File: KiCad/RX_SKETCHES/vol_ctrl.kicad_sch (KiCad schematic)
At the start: 6 parts

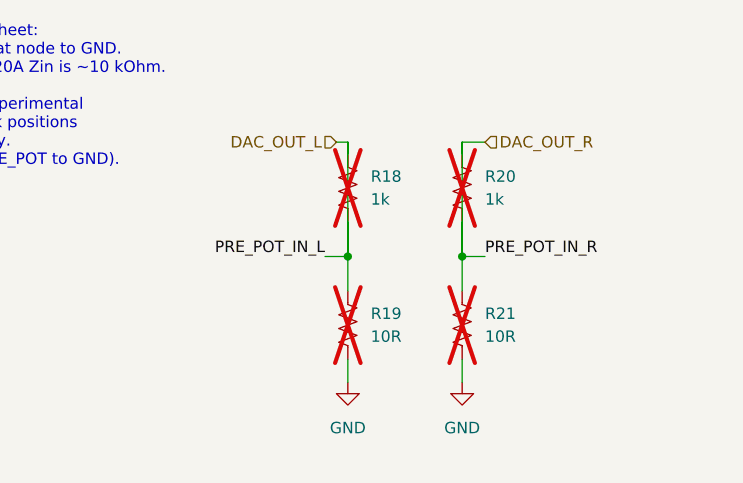
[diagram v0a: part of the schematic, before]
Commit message: WIP: RX schematic review — restore DAC/amp, fix ESP nets, log revisions.
Restore dac/amp from main after rotate damage, rename I2S net to DOUT,
mark amp gain Rs DNP, and record change/rationale in docs/hardware_revisions.org.

Co-authored-by: Cursor <cursoragent@cursor.com>
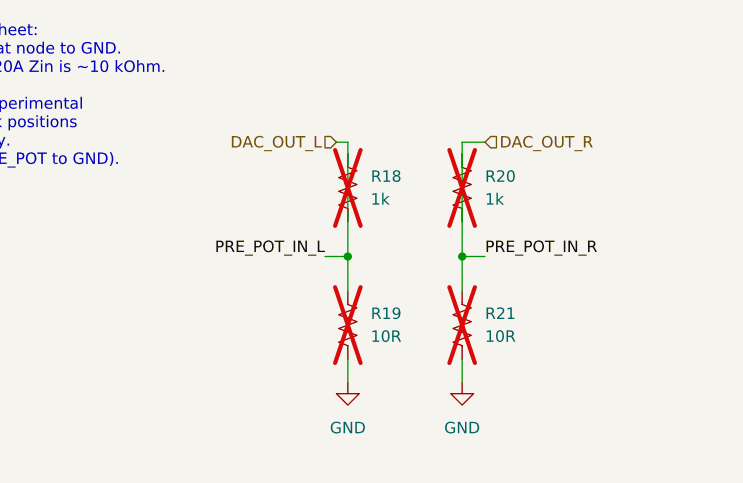
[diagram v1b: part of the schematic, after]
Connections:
- net DAC_OUT_L: no longer R18.1, R18.2
- net DAC_OUT_R: no longer R20.1, R20.2
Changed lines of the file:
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@@
 		(comment 4 "POST_POT_IN_R/L becomes the input to the amp.")
+	)
+	(text "PCM5102 datasheet filter lives on the DAC sheet:\nDAC_OUT -- 470R -- PRE_POT, 2.2nF from that node to GND.\nThat network assumes ~10 kOhm. MAX97220A Zin is ~10 kOhm.\n\nR18/R20 1k and R19/R21 10R are the old experimental\n40 dB pad. They are DNP. Wires short the 1k positions\nso the pot sees the filtered DAC_OUT directly.\nLeave the 10R pads empty (do not shunt PRE_POT to GND)."
+		(exclude_from_sim no)
+		(at 20.32 20.32 0)
+		(effects
+			(font
+				(size 1.27 1.27)
+			)
+			(justify left)
+		)
 	)
 	(junction
@@
 		(pts
 			(xy 121.92 78.74) (xy 120.65 78.74)
-		)
-		(stroke
-			(width 0)
-			(type default)
-		)
-	)
-	(wire
-		(pts
-			(xy 97.79 25.4) (xy 97.79 26.67)
 		)
 		(stroke
@@
 	(wire
 		(pts
-			(xy 110.49 34.29) (xy 110.49 38.1)
-		)
-		(stroke
-			(width 0)
-			(type default)
-		)
-	)
-	(wire
-		(pts
 			(xy 121.92 83.82) (xy 123.19 83.82)
 		)
@@
 	(wire
 		(pts
-			(xy 97.79 34.29) (xy 97.79 38.1)
+			(xy 97.79 25.4) (xy 97.79 38.1)
 		)
 		(stroke
@@
 	(wire
 		(pts
-			(xy 110.49 25.4) (xy 110.49 26.67)
+			(xy 110.49 49.53) (xy 110.49 52.07)
 		)
 		(stroke
@@
 	(wire
 		(pts
-			(xy 110.49 49.53) (xy 110.49 52.07)
+			(xy 110.49 25.4) (xy 110.49 38.1)
 		)
 		(stroke
@@
 		)
 	)
-	(wire
-		(pts
-			(xy 97.79 25.4) (xy 97.79 38.1)
-		)
-		(stroke
-			(width 0)
-			(type default)
-		)
-	)
-	(wire
-		(pts
-			(xy 110.49 25.4) (xy 110.49 38.1)
-		)
-		(stroke
-			(width 0)
-			(type default)
-		)
-	)
-	(text "PCM5102 datasheet filter lives on the DAC sheet:\nDAC_OUT -- 470R -- PRE_POT, 2.2nF from that node to GND.\nThat network assumes ~10 kOhm. MAX97220A Zin is ~10 kOhm.\n\nR18/R20 1k and R19/R21 10R are the old experimental\n40 dB pad. They are DNP. Wires short the 1k positions\nso the pot sees the filtered DAC_OUT directly.\nLeave the 10R pads empty (do not shunt PRE_POT to GND)."
-		(exclude_from_sim no)
-		(at 20.32 20.32 0)
-		(effects
-			(font
-				(size 1.27 1.27)
-			)
-			(justify left)
-		)
-	)

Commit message: RX: finish layout, retune gain/coupling, move ESD clamp to unswitched VBUS
Board now passes DRC with zero unconnected items and zero schematic-parity
issues. Remaining 16 violations are footprint-inherent (ESP32 module thermal
via array at 0.2 mm drill, USB-C NPTH-to-pad spacing) and are documented
rather than routed around.

Analog changes, with the reasoning captured in README.org and
docs/hardware_revisions.org so the numbers can be re-checked:

- Gain network populated at RF 4.7k / RIN 47k (-20 dB) instead of DNP 10k.
  Tames the DAC's 2.1 Vrms into sensitive IEMs, unloads the pot taper, and
  moves the coupling corner out of the audible band.
- Coupling caps C1-C4 0.47uF -> 1uF. Corner 7.2 Hz -> 3.4 Hz, and it halves
  the signal developed across the ceramic at 20 Hz, cutting Class-II
  dielectric distortion where it actually occurs.
- D1's third TVS channel moved off the switched +5V rail onto VBUS_RAW. The
  clamp has to sit on the connector pin that is exposed to a finger; behind
  the power switch it went open exactly when the board is most handled.
- SW3 soft mute: XSMT_SEL moved to the throw that puts mute on the south
  slide position. All three switches now follow one rule -- the open throw
  is the safe default (off / quality filter / muted).
- PCM5102 mode pins no longer float: FLT and XSMT get 100k pulldowns, DEMP
  and FMT strap to GND.
- C28 and the four mounting holes added to the schematic to clear parity
  errors against parts that only existed on the PCB.

Also adds a .gitignore so the 24 MB editor .history/ directory and ESP-IDF
build output stop showing up as untracked.

Co-authored-by: Cursor <cursoragent@cursor.com>
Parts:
- removed R18, R20: 1k, Resistor_SMD:R_0805_2012Metric_Pad1.20x1.40mm_HandSolder, symbol Device:R_US
- removed R19, R21: 10R, Resistor_SMD:R_0805_2012Metric_Pad1.20x1.40mm_HandSolder, symbol Device:R_US
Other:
- note added: "DRIVE SHDN_SIGNAL HIGH FOR NORMAL OPERATION"
- note added: "PCM5102 datasheet filter lives on the DAC sheet: DAC_OUT -- 470R -- PRE_POT, 2.2nF from that node to GND. That network assumes ~10 kOhm. MAX97220A Zin is ~10 kOhm. MAX_VOL will be set by R_IN and R_F. R_IN will stay at 10k but can change R_F as needed to ensure safe volume during operation."
- note removed: "PCM5102 datasheet filter lives on the DAC sheet: DAC_OUT -- 470R -- PRE_POT, 2.2nF from that node to GND. That network assumes ~10 kOhm. MAX97220A Zin is ~10 kOhm. R18/R20 1k and R19/R21 10R are the old experimental 40 dB pad. They are DNP. Wires short the 1k positions so the pot sees the filtered DAC_OUT directly. Leave the 10R pads empty (do not shunt PRE_POT to GND)."
- moved on the sheet: R22, VR1
